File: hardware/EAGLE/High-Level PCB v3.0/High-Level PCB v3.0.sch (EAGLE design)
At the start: 54 parts, among them IC1 MCP2551, IC2 DS8921, IC3 DS8921, J1 Optical Mouse, J2 GPS, J3 Gyro, J4 Micro-SD, J5 Compass, J6 Compass, J7 ODO_JACK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

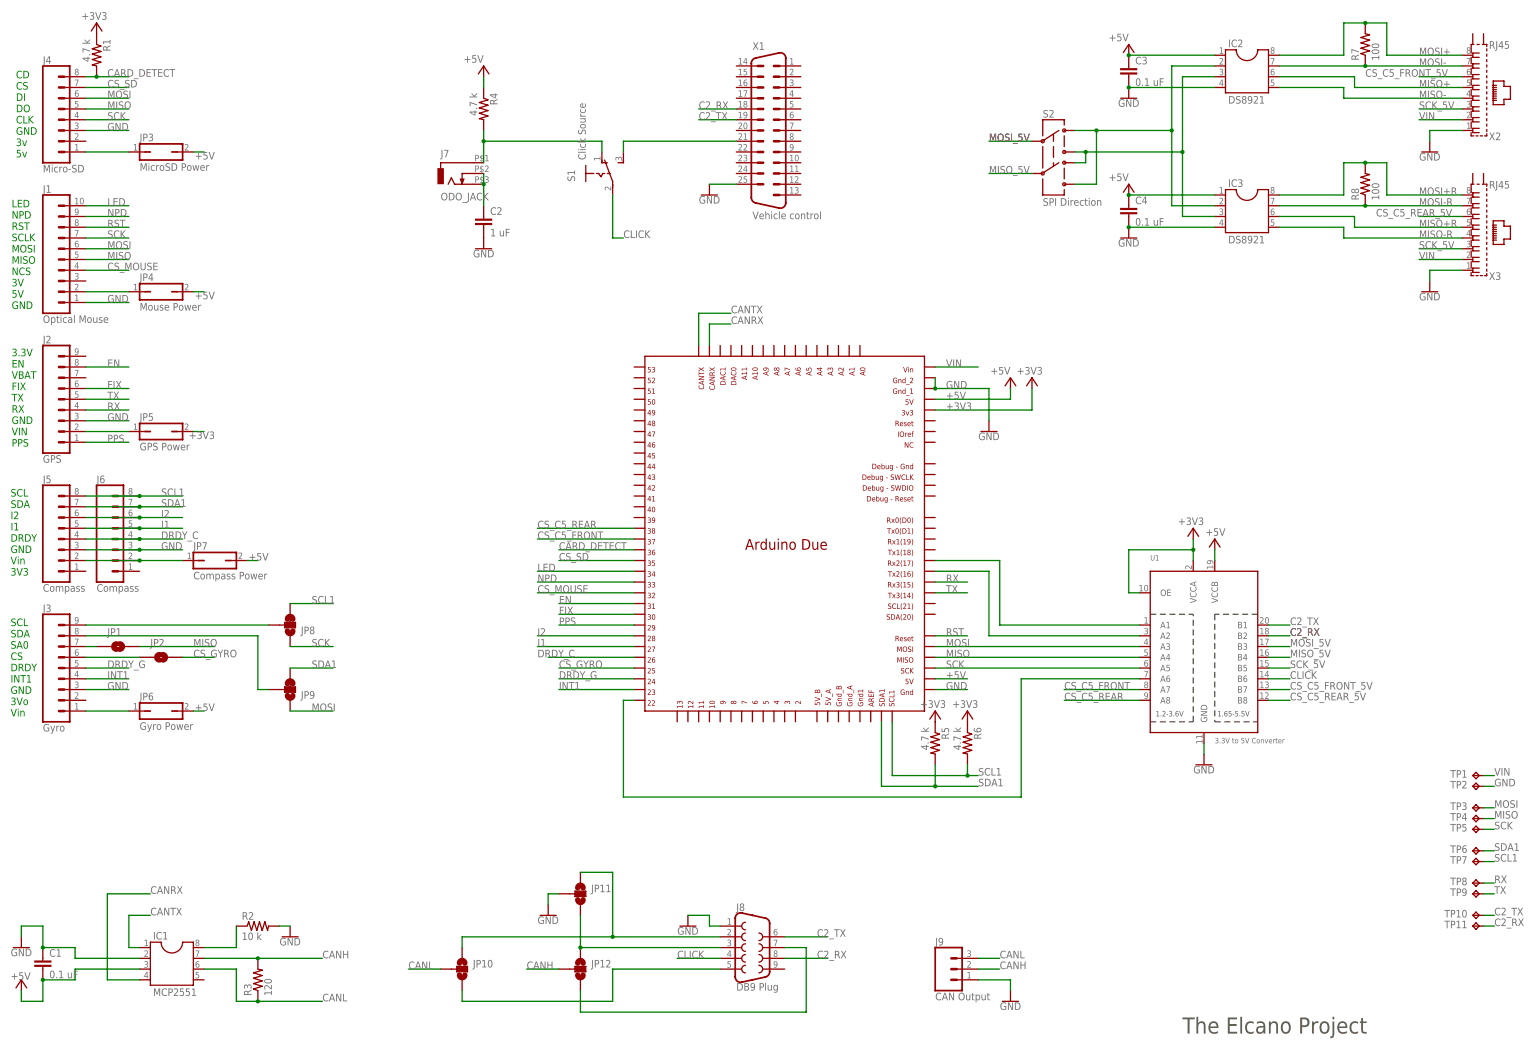
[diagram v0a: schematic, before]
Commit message: Added Test Points for +5V and +3V3
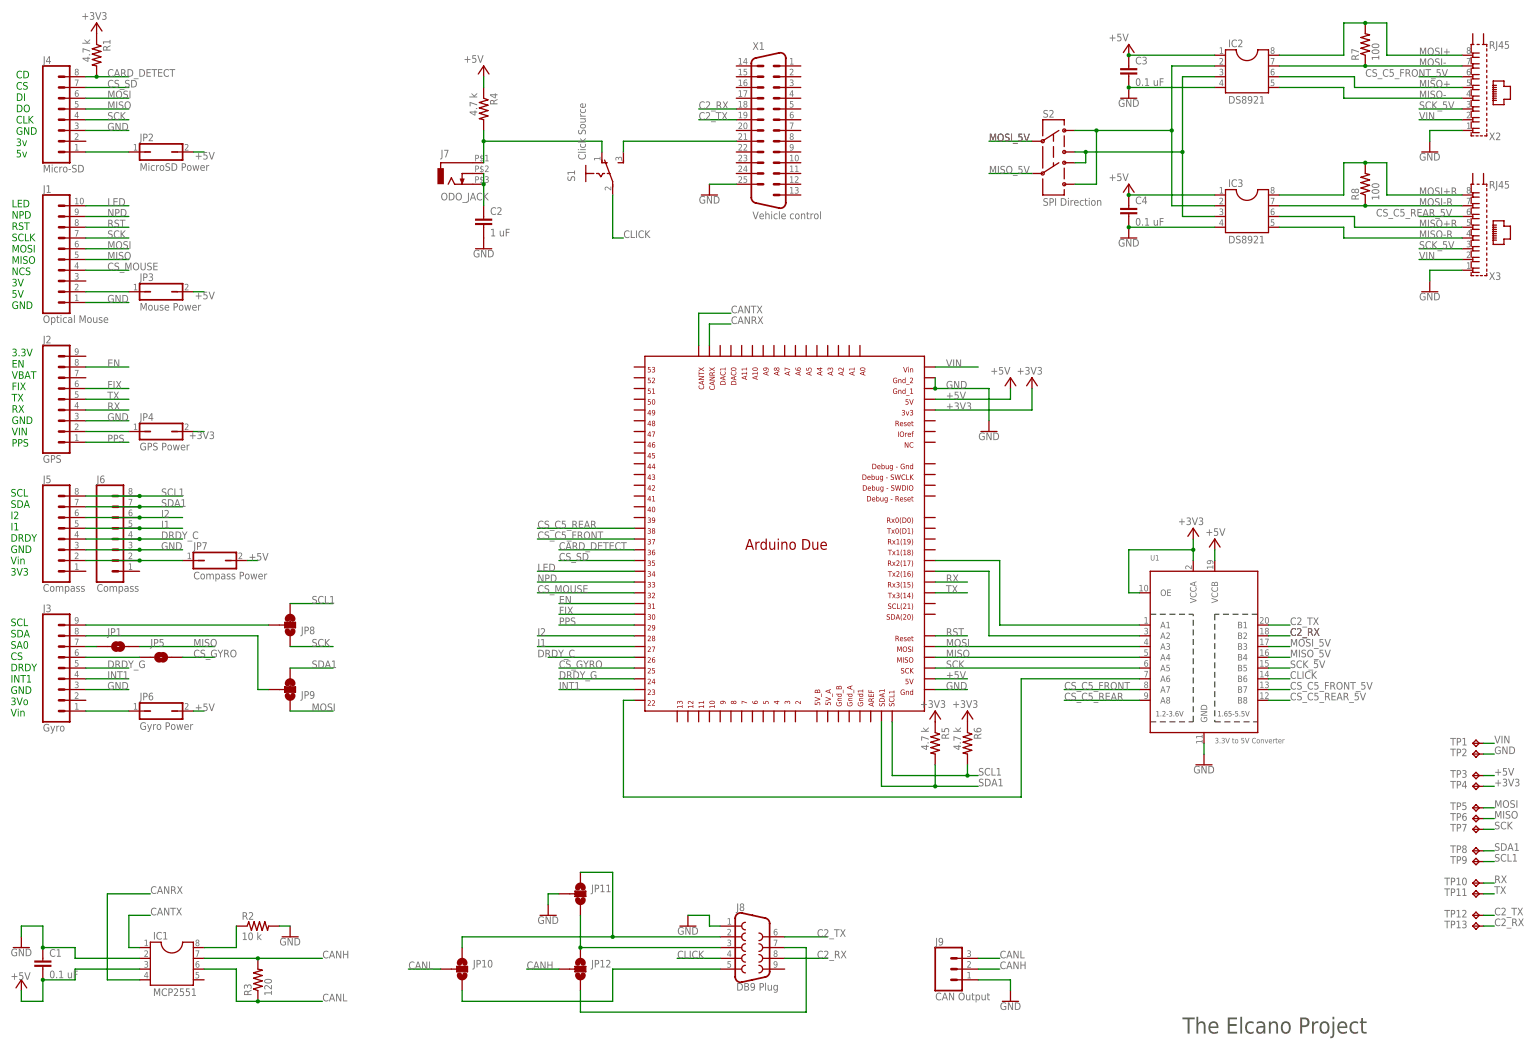
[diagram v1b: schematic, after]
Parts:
- added TP12, TP13: TPPAD1-17, testpad:TPPAD1-17
- JP2: value JUMPER-SMT_2_NO_SILK -> MicroSD Power; device SparkFun-Jumpers:JUMPER-SMT_2_NO_SILK -> jumper:JP1Q
- JP3: value MicroSD Power -> Mouse Power
- JP4: value Mouse Power -> GPS Power
- JP5: value GPS Power -> JUMPER-SMT_2_NO_SILK; device jumper:JP1Q -> SparkFun-Jumpers:JUMPER-SMT_2_NO_SILK
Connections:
- net +3V3: now also JP4.2, TP4.TP; no longer JP5.2
- net +5V: now also JP2.2, TP3.TP; no longer JP4.2
- net C2_RX: now also TP13.TP; no longer TP11.TP
- net C2_TX: now also TP12.TP; no longer TP10.TP
- net CS_GYRO: now also JP5.2; no longer JP2.2
- net MISO: now also TP6.TP; no longer TP4.TP
- net MOSI: now also TP5.TP; no longer TP3.TP
- net N$10: now also JP2.1; no longer JP3.1
- net N$13: now also JP3.1; no longer JP4.1
- net N$14: now also JP4.1; no longer JP5.1
- net N$19: now also JP5.1; no longer JP2.1
- net RX: now also TP10.TP; no longer TP8.TP
- net SCK: now also TP7.TP; no longer TP5.TP
- net SCL1: now also TP9.TP; no longer TP7.TP
- net SDA1: now also TP8.TP; no longer TP6.TP
- net TX: now also TP11.TP; no longer TP9.TP
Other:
- moved on the sheet: JP3, JP4, TP1, TP10, TP11, TP2, TP3, TP4, TP5, TP6, TP7, TP8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

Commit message: Add files via upload
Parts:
- removed J2: GPS, SparkFun-Connectors:CONN_09
- removed U1: 3.3V to 5V Converter, TXb0108:TXB0108PWR
- added GPS: ELGPS, ELGPS:ELGPS
- added U2: (no value), ELSHIFTER:ELSHIFTER
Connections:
- net +3V3: now also U2.OE, U2.VCCA; no longer U1.OE, U1.VCCA
- net +5V: now also U2.VCCB; no longer U1.VCCB
- net C2_RX: now also U2.B2; no longer U1.B2
- net C2_TX: now also U2.B1; no longer U1.B1
- net CLICK: now also U2.B6; no longer U1.B6
- net CS_C5_FRONT: now also U2.A7; no longer U1.A7
- net CS_C5_FRONT_5V: now also U2.B7; no longer U1.B7
- net CS_C5_REAR: now also U2.A8; no longer U1.A8
- net CS_C5_REAR_5V: now also U2.B8; no longer U1.B8
- net EN: now also GPS.EN; no longer J2.8
- net FIX: now also GPS.FIX; no longer J2.6
- net GND: now also GPS.GND, U2.GND; no longer J2.3, U1.GND
- net MISO: now also U2.A4; no longer U1.A4
- net MISO_5V: now also U2.B4; no longer U1.B4
- net MOSI: now also U2.A3; no longer U1.A3
- net MOSI_5V: now also U2.B3; no longer U1.B3
- net N$12: now also U2.A6; no longer U1.A6
- net N$14: now also GPS.VIN; no longer J2.2
- net N$4: now also U2.A2; no longer U1.A2
- net N$5: now also U2.A1; no longer U1.A1
- net PPS: now also GPS.PPS; no longer J2.1
- net RX: now also GPS.RX; no longer J2.4
- net SCK: now also U2.A5; no longer U1.A5
- net SCK_5V: now also U2.B5; no longer U1.B5
- net TX: now also GPS.TX; no longer J2.5
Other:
- note removed: "3.3V EN VBAT FIX TX RX GND VIN PPS"

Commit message: Add files via upload
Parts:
- removed J5, J6: Compass, SparkFun-Connectors:CONN_08"
- added U1: COMPASS, ELCOMPASS:ELCOMPASS
- added U4: (no value), ELCOMPASS:ELCOMPASS
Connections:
- net DRDY_C: now also U1.DRDY, U4.DRDY; no longer J5.4, J6.4
- net GND: now also U1.GND, U4.GND; no longer J5.3, J6.3
- net I1: now also U1.I1, U4.I1; no longer J5.5, J6.5
- net I2: now also U1.I2, U4.I2; no longer J5.6, J6.6
- net N$8: now also U1.VIN, U4.VIN; no longer J5.2, J6.2
- net SCL1: now also U1.SCL, U4.SCL; no longer J5.8, J6.8
- net SDA1: now also U1.SDA, U4.SDA; no longer J5.7, J6.7
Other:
- note removed: "SCL SDA I2 I1 DRDY GND Vin 3V3"
- moved on the sheet: J3, JP1, JP5, JP6, JP7, JP8, JP9

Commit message: Add files via upload
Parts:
- removed GPS: ELGPS, ELGPS:ELGPS
- added U3: GPS, ELGPS:ELGPS
- U2: value (none) -> LLSHIFTER
- U4: value (none) -> COMPASS
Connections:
- net EN: now also U3.EN; no longer GPS.EN
- net FIX: now also U3.FIX; no longer GPS.FIX
- net GND: now also U3.GND; no longer GPS.GND
- net N$14: now also U3.VIN; no longer GPS.VIN
- net PPS: now also U3.PPS; no longer GPS.PPS
- net RX: now also U3.RX; no longer GPS.RX
- net TX: now also U3.TX; no longer GPS.TX
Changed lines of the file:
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@@
 <part name="TP1" library="testpad" library_urn="urn:adsk.eagle:library:385" deviceset="TP" device="PAD1-17" package3d_urn="urn:adsk.eagle:package:27949/1"/>
 <part name="TP2" library="testpad" library_urn="urn:adsk.eagle:library:385" deviceset="TP" device="PAD1-17" package3d_urn="urn:adsk.eagle:package:27949/1"/>
-<part name="U2" library="ELSHIFTER" deviceset="ELSHIFTER" device=""/>
-<part name="GPS" library="ELGPS" deviceset="ELGPS" device="" value="ELGPS">
-<attribute name="SPICEPREFIX" value="X"/>
-</part>
+<part name="U2" library="ELSHIFTER" deviceset="ELSHIFTER" device="" value="LLSHIFTER"/>
 <part name="U1" library="ELCOMPASS" deviceset="ELCOMPASS" device="" value="COMPASS"/>
-<part name="U4" library="ELCOMPASS" deviceset="ELCOMPASS" device=""/>
+<part name="U4" library="ELCOMPASS" deviceset="ELCOMPASS" device="" value="COMPASS"/>
+<part name="U3" library="ELGPS" deviceset="ELGPS" device="" value="GPS"/>
 </parts>
 <sheets>
@@
 </instance>
 <instance part="U2" gate="G$1" x="284.48" y="78.74"/>
-<instance part="GPS" gate="G$1" x="17.78" y="144.78" rot="MR0"/>
 <instance part="U1" gate="G$1" x="30.48" y="101.6" rot="MR0"/>
 <instance part="U4" gate="G$1" x="60.96" y="127" rot="R90"/>
+<instance part="U3" gate="G$1" x="27.94" y="144.78" rot="MR0"/>
 </instances>
 <busses>
@@
 <wire x1="33.02" y1="152.4" x2="43.18" y2="152.4" width="0.1524" layer="91"/>
 <label x="38.1" y="152.4" size="1.778" layer="95"/>
-<pinref part="GPS" gate="G$1" pin="GND"/>
+<pinref part="U3" gate="G$1" pin="GND"/>
 </segment>
 <segment>
@@
 <wire x1="33.02" y1="160.02" x2="43.18" y2="160.02" width="0.1524" layer="91"/>
 <label x="38.1" y="160.02" size="1.778" layer="95"/>
-<pinref part="GPS" gate="G$1" pin="FIX"/>
+<pinref part="U3" gate="G$1" pin="FIX"/>
 </segment>
 <segment>
@@
 <wire x1="33.02" y1="157.48" x2="43.18" y2="157.48" width="0.1524" layer="91"/>
 <label x="38.1" y="157.48" size="1.778" layer="95"/>
-<pinref part="GPS" gate="G$1" pin="TX"/>
+<pinref part="U3" gate="G$1" pin="TX"/>
 </segment>
 <segment>
@@
 <wire x1="33.02" y1="154.94" x2="43.18" y2="154.94" width="0.1524" layer="91"/>
 <label x="38.1" y="154.94" size="1.778" layer="95"/>
-<pinref part="GPS" gate="G$1" pin="RX"/>
+<pinref part="U3" gate="G$1" pin="RX"/>
 </segment>
 <segment>
@@
 <wire x1="33.02" y1="147.32" x2="43.18" y2="147.32" width="0.1524" layer="91"/>
 <label x="38.1" y="147.32" size="1.778" layer="95"/>
-<pinref part="GPS" gate="G$1" pin="PPS"/>
+<pinref part="U3" gate="G$1" pin="PPS"/>
 </segment>
 <segment>
@@
 <pinref part="JP4" gate="A" pin="1"/>
 <wire x1="43.18" y1="149.86" x2="33.02" y2="149.86" width="0.1524" layer="91"/>
-<pinref part="GPS" gate="G$1" pin="VIN"/>
+<pinref part="U3" gate="G$1" pin="VIN"/>
 </segment>
 </net>
@@
 <wire x1="33.02" y1="165.1" x2="43.18" y2="165.1" width="0.1524" layer="91"/>
 <label x="38.1" y="165.1" size="1.778" layer="95"/>
-<pinref part="GPS" gate="G$1" pin="EN"/>
-</segment>
-<segment>
+<pinref part="U3" gate="G$1" pin="EN"/>
+</segment>
+<segment>
